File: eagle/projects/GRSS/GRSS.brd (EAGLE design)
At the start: 66 x 62.1 mm, 38 parts, among them J1 MOL-SL-2-RA, J10 MOL-SL-2-RA, J11 MOL-SL-2-V, J2 MOL-SL-2-RA, J3 MOL-SL-2-RA, J4 MOL-SL-2-RA, J5 MOL-SL-2-RA, J6 MOL-SL-2-RA, J7 MOL-SL-2-RA, J8 MOL-SL-2-RA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

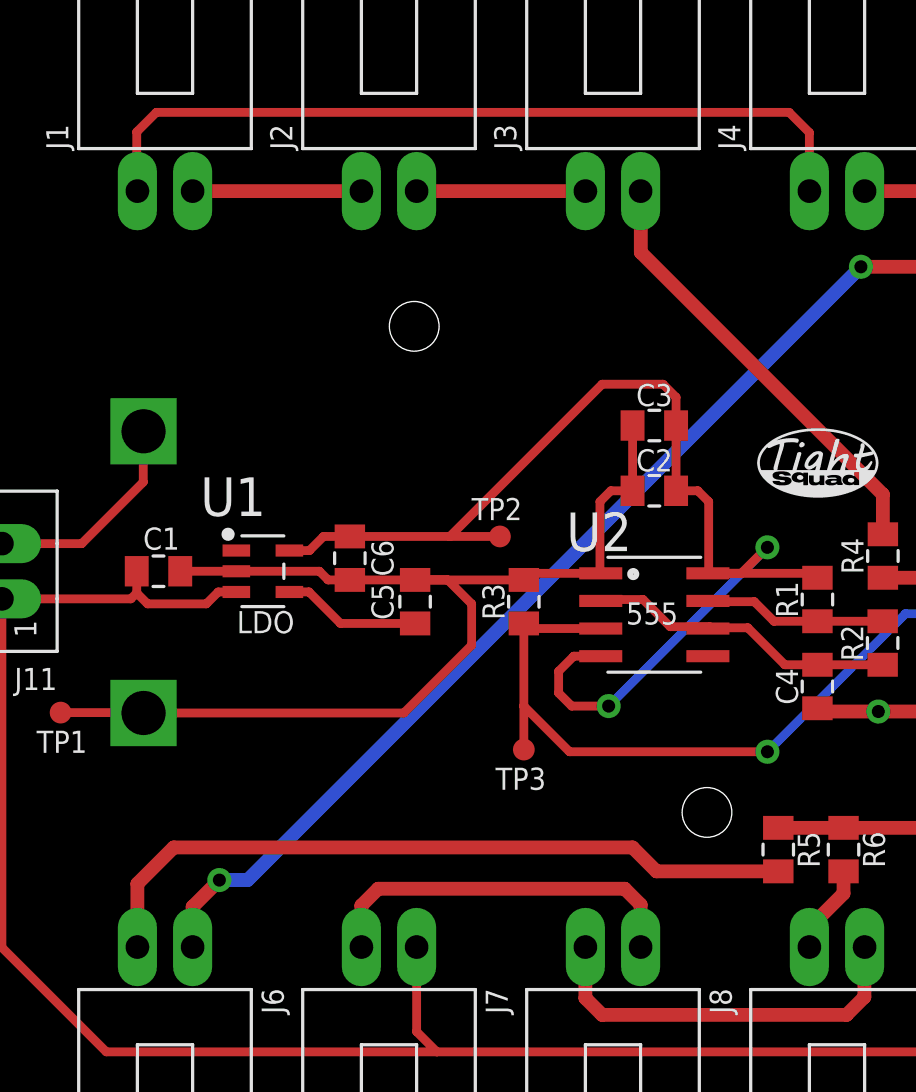
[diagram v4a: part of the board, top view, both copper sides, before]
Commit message: added tyrap holes / updated silkscreen of battery
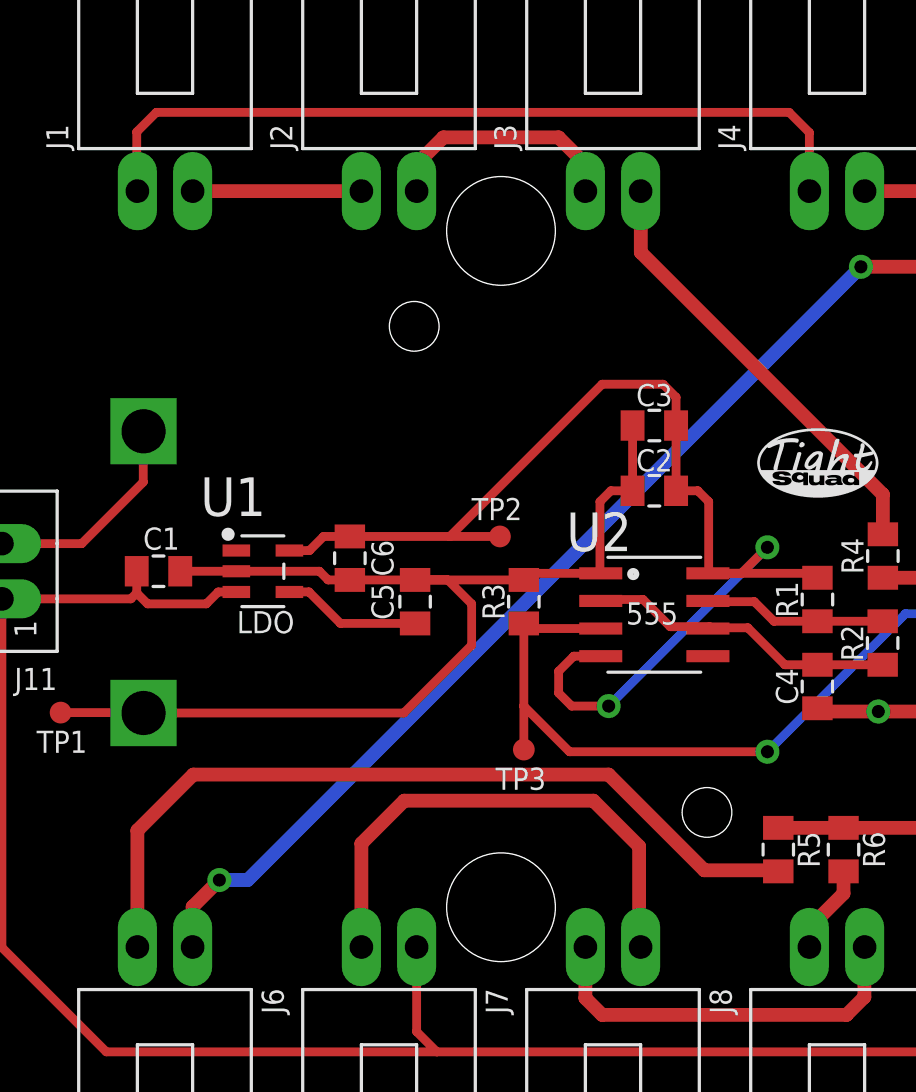
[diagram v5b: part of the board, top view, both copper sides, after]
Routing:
- net LED78: track 17.3 -> 23.9 mm
- net RES456: track 33.5 -> 37.7 mm
- net LED23: track 7.76 -> 11.3 mm
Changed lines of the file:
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@@
 <layer number="17" name="Pads" color="2" fill="1" visible="yes" active="yes"/>
 <layer number="18" name="Vias" color="2" fill="1" visible="yes" active="yes"/>
-<layer number="19" name="Unrouted" color="6" fill="1" visible="no" active="yes"/>
+<layer number="19" name="Unrouted" color="6" fill="1" visible="yes" active="yes"/>
 <layer number="20" name="Dimension" color="15" fill="1" visible="yes" active="yes"/>
 <layer number="21" name="tPlace" color="7" fill="1" visible="yes" active="yes"/>
@@
 XXX-XXX-XX</text>
 <text x="58.54" y="7.6" size="1.016" layer="21" ratio="15">Buzzer</text>
+<hole x="28.35" y="46.6" drill="5"/>
+<hole x="28.35" y="15.5" drill="5"/>
 </plain>
 <attributes>
@@
 <contactref element="R5" pad="2"/>
 <contactref element="J6" pad="2"/>
-<wire x1="11.63" y1="13.67" x2="11.63" y2="16.58" width="0.635" layer="1"/>
-<wire x1="11.63" y1="16.58" x2="13.3" y2="18.25" width="0.635" layer="1"/>
-<wire x1="13.3" y1="18.25" x2="34.4" y2="18.25" width="0.635" layer="1"/>
-<wire x1="34.4" y1="18.25" x2="35.5" y2="17.15" width="0.635" layer="1"/>
-<wire x1="35.5" y1="17.15" x2="41.1" y2="17.15" width="0.635" layer="1"/>
+<wire x1="11.63" y1="13.67" x2="11.63" y2="19.03" width="0.635" layer="1"/>
+<wire x1="11.63" y1="19.03" x2="14.2" y2="21.6" width="0.635" layer="1"/>
+<wire x1="14.2" y1="21.6" x2="33.3" y2="21.6" width="0.635" layer="1"/>
+<wire x1="33.3" y1="21.6" x2="37.7" y2="17.2" width="0.635" layer="1"/>
+<wire x1="37.7" y1="17.2" x2="41.05" y2="17.2" width="0.635" layer="1"/>
+<wire x1="41.05" y1="17.2" x2="41.1" y2="17.15" width="0.635" layer="1"/>
 </signal>
 <signal name="LED89">
@@
 <contactref element="J2" pad="2"/>
 <contactref element="J3" pad="1"/>
-<wire x1="24.47" y1="48.43" x2="32.23" y2="48.43" width="0.635" layer="1"/>
+<wire x1="24.47" y1="48.43" x2="24.47" y2="49.67" width="0.635" layer="1"/>
+<wire x1="24.47" y1="49.67" x2="25.7" y2="50.9" width="0.635" layer="1"/>
+<wire x1="25.7" y1="50.9" x2="31" y2="50.9" width="0.635" layer="1"/>
+<wire x1="31" y1="50.9" x2="32.2" y2="49.7" width="0.635" layer="1"/>
+<wire x1="32.2" y1="49.7" x2="32.2" y2="48.46" width="0.635" layer="1"/>
+<wire x1="32.2" y1="48.46" x2="32.23" y2="48.43" width="0.635" layer="1"/>
 </signal>
 <signal name="LED12">
@@
 <contactref element="J7" pad="2"/>
 <contactref element="J8" pad="1"/>
-<wire x1="21.93" y1="13.67" x2="21.93" y2="15.58" width="0.635" layer="1"/>
-<wire x1="21.93" y1="15.58" x2="22.7" y2="16.35" width="0.635" layer="1"/>
-<wire x1="22.7" y1="16.35" x2="34.04" y2="16.35" width="0.635" layer="1"/>
-<wire x1="34.04" y1="16.35" x2="34.77" y2="15.62" width="0.635" layer="1"/>
-<wire x1="34.77" y1="15.62" x2="34.77" y2="13.67" width="0.635" layer="1"/>
+<wire x1="21.93" y1="13.67" x2="21.93" y2="18.43" width="0.635" layer="1"/>
+<wire x1="21.93" y1="18.43" x2="23.9" y2="20.4" width="0.635" layer="1"/>
+<wire x1="23.9" y1="20.4" x2="32.6" y2="20.4" width="0.635" layer="1"/>
+<wire x1="32.6" y1="20.4" x2="34.7" y2="18.3" width="0.635" layer="1"/>
+<wire x1="34.7" y1="18.3" x2="34.7" y2="13.74" width="0.635" layer="1"/>
+<wire x1="34.7" y1="13.74" x2="34.77" y2="13.67" width="0.635" layer="1"/>
 </signal>
 <signal name="NC">

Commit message: Layout RevB -- All of Mark's revs complete
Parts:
- moved LOGO1 2.28 mm to (38.0, 33.4)
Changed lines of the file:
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@@
 <attribute name="VALUE" x="49.56" y="23.5" size="0.254" layer="27" ratio="6" align="center"/>
 </element>
-<element name="LOGO1" library="grss" package="SQUAD_LOGO" value="LOGO" x="40.1" y="34.3">
-<attribute name="_EXTERNAL_" value="" x="40.1" y="34.3" size="1.778" layer="27" display="off"/>
+<element name="LOGO1" library="grss" package="SQUAD_LOGO" value="LOGO" x="38" y="33.4">
+<attribute name="_EXTERNAL_" value="" x="38" y="33.4" size="1.778" layer="27" display="off"/>
 </element>
 <element name="E$1" library="grss" package="LG" value="" x="59.6" y="32.6"/>
@@
 <wire x1="11.63" y1="13.67" x2="11.63" y2="19.03" width="0.635" layer="1"/>
 <wire x1="11.63" y1="19.03" x2="14.2" y2="21.6" width="0.635" layer="1"/>
-<wire x1="14.2" y1="21.6" x2="33.3" y2="21.6" width="0.635" layer="1"/>
-<wire x1="33.3" y1="21.6" x2="37.7" y2="17.2" width="0.635" layer="1"/>
-<wire x1="37.7" y1="17.2" x2="41.05" y2="17.2" width="0.635" layer="1"/>
+<wire x1="14.2" y1="21.6" x2="33.1" y2="21.6" width="0.635" layer="1"/>
+<wire x1="33.1" y1="21.6" x2="37.5" y2="17.2" width="0.635" layer="1"/>
+<wire x1="37.5" y1="17.2" x2="41.05" y2="17.2" width="0.635" layer="1"/>
 <wire x1="41.05" y1="17.2" x2="41.1" y2="17.15" width="0.635" layer="1"/>
 </signal>
